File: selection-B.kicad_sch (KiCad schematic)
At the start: 11 parts, among them Q2 DMG2302U-7, Q3 DMG2302U-7, Q4 DMG2302U-7, Q5 DMG2302U-7, U11 SN74LS08N, U12 SN74LS08N, U13 CD74HCT32E, U9 SN74LS08N

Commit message: feat: added point_tests + fixed wrong footprint for switch + added anime girl
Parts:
- added OUT_SEL_ADD_B0, OUT_SEL_ADD_B1, OUT_SEL_ADD_B2, OUT_SEL_ADD_B3, OUT_SEL_MUL_B0, OUT_SEL_MUL_B1: TestPoint, TestPoint:TestPoint_THTPad_D1.0mm_Drill0.5mm, symbol Connector:TestPoint
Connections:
- net OUT_ADD_B0: now also OUT_SEL_ADD_B0.1
- net OUT_ADD_B1: now also OUT_SEL_ADD_B1.1
- net OUT_ADD_B2: now also OUT_SEL_ADD_B2.1
- net OUT_ADD_B3: now also OUT_SEL_ADD_B3.1
- net OUT_MUL_B0: now also OUT_SEL_MUL_B0.1
- net OUT_MUL_B1: now also OUT_SEL_MUL_B1.1

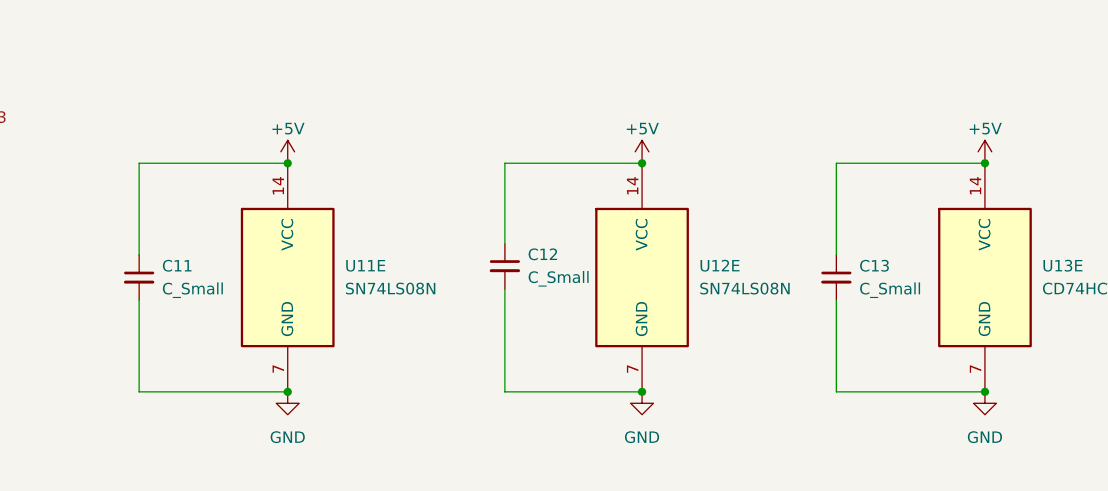
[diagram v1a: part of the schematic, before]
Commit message: chore: changed R and C ref to passive value
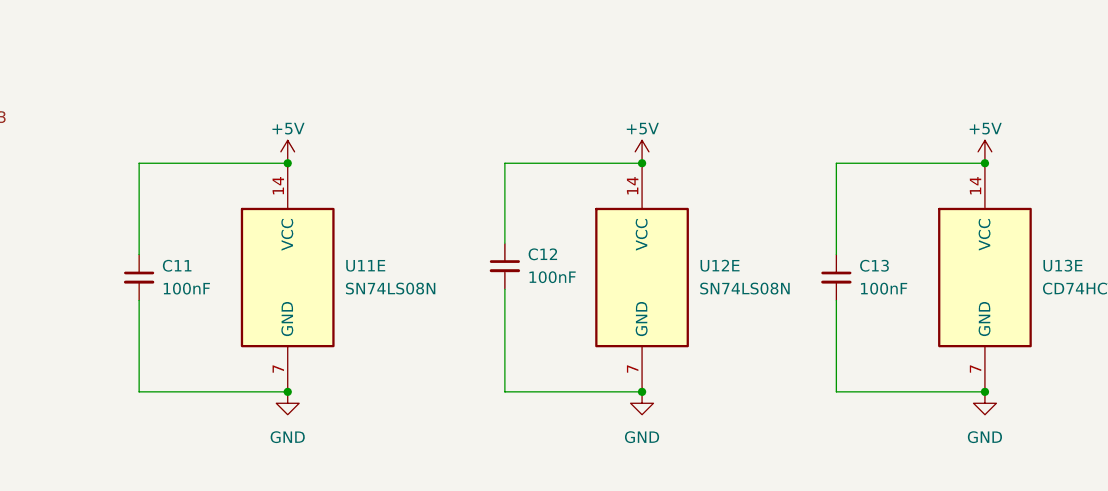
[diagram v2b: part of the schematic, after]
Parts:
- C11, C12, C13: value C_Small -> 100nF
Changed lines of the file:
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@@
 			)
 		)
-		(property "Value" "C_Small"
+		(property "Value" "100nF"
 			(at 214.63 143.5162 0)
 			(effects
@@
 			)
 		)
-		(property "Value" "C_Small"
+		(property "Value" "100nF"
 			(at 251.46 144.7862 0)
 			(effects
@@
 			)
 		)
-		(property "Value" "C_Small"
+		(property "Value" "100nF"
 			(at 173.99 144.7862 0)
 			(effects
